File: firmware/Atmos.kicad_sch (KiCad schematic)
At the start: 42 parts, among them J1 AS3935 breakout, J2 BME280 breakout, J3 USB_C_Receptacle_USB2.0_16P, J4 Micro_SD_Card, J5 Solar power input, J6 Conn_Coaxial, Q1 PMOS_Substrate, Q2 PMOS_Substrate, SW2 SW_Push, U1 ESP32-S3-WROOM-1, U10 TPS22918DBVR, U11 MAX17048G_T10, U12 CN3791, U13 SGP40-D-R4, U2 AP2112K-3.3, U3 DS3231M, U4 PMS5003, U5 LTC4412xS6, U7 RFM95W-915S2, U8 USBLC6-2SC6, U9 TPS61023DRLR

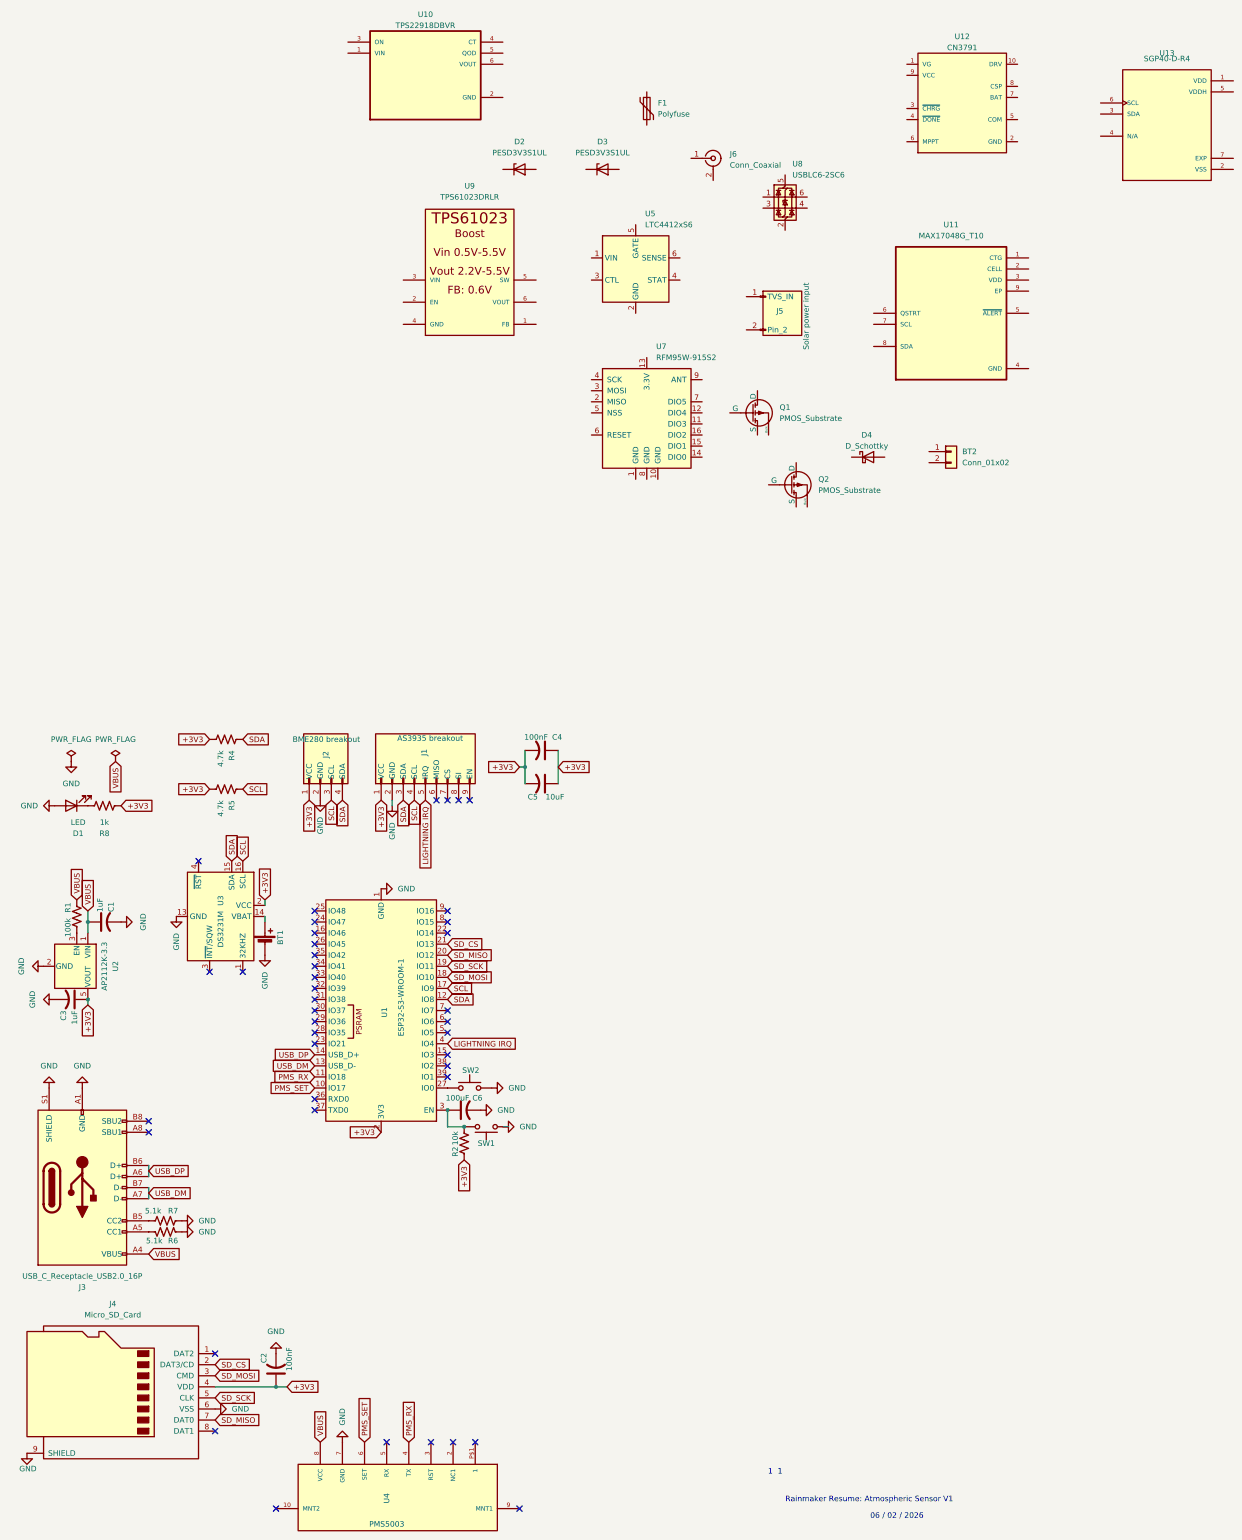
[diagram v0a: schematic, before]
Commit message: Sync latest schematic + add AI exports (PDF/netlist/BOM) for browser-Claude
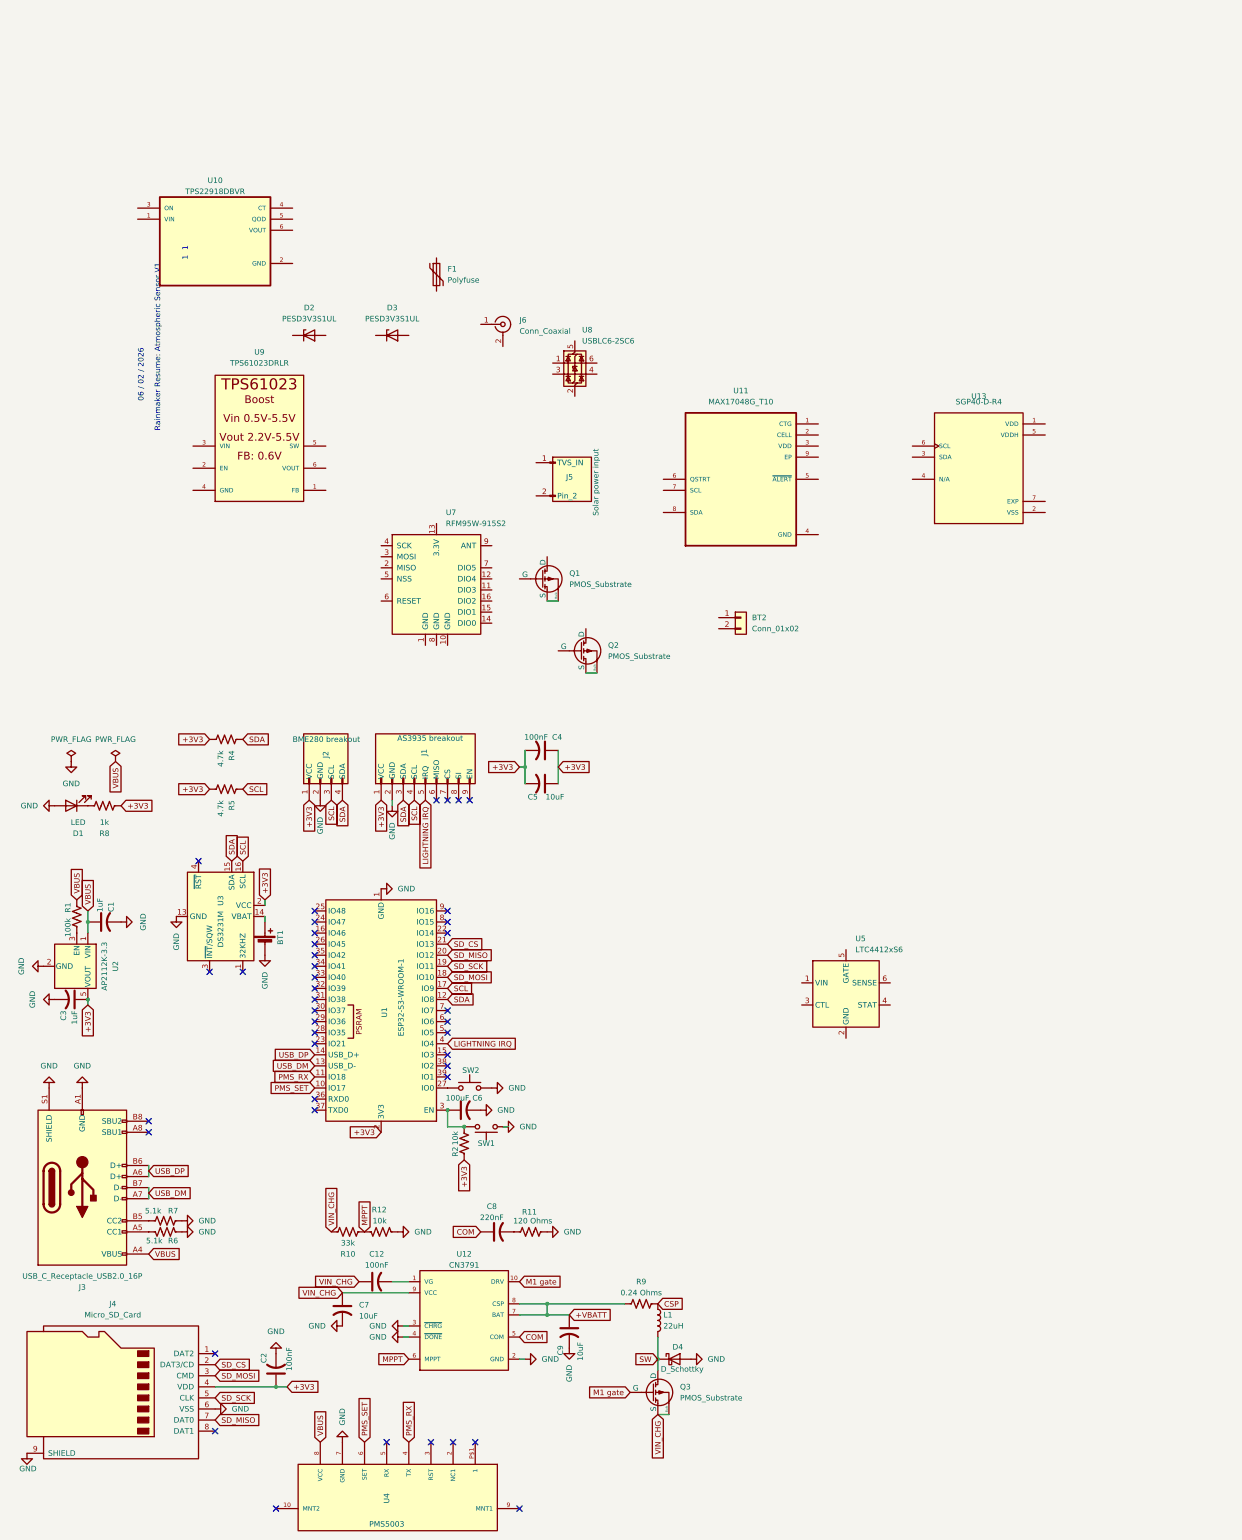
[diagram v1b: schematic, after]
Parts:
- added C12: 100nF, symbol Device:C_US
- added C7, C9: 10uF, symbol Device:C_US
- added C8: 220nF, symbol Device:C_US
- added L1: 22uH, symbol Device:L
- added Q3: PMOS_Substrate, symbol Simulation_SPICE:PMOS_Substrate
- added R10: 33k, symbol Device:R_US
- added R11: 120 Ohms, symbol Device:R_US
- added R12: 10k, symbol Device:R_US
- added R9: 0.24 Ohms, symbol Device:R_US
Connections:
- net GND: now also D4.2 (A), U12.2 (GND), U12.3 (~{CHRG}), U12.4 (~{DONE}), C7.2, C9.2, R11.2, R12.2
- net at Q2.3 (S): now also Q2.4 (Bulk)
- net at Q1.3 (S): now also Q1.4 (Bulk)
- net at U12.1 (VG): now also C12.2
- net M1 gate: now reaches U12.10 (DRV)
- net M1 gate: now also Q3.2 (G)
- net COM: now reaches U12.5 (COM)
- net COM: now also C8.1
- net MPPT: now reaches U12.6 (MPPT)
- net MPPT: now also R10.1, R12.1
- net +VBATT: now reaches U12.7 (BAT)
- net +VBATT: now also U12.8 (CSP), C9.1, R9.1
- net VIN_CHG: now reaches U12.9 (VCC)
- net VIN_CHG: now also C12.1, C7.1, Q3.3 (S), Q3.4 (Bulk), R10.2
- net SW: now reaches D4.1 (K)
- net SW: now also L1.2, Q3.1 (D)
- new net: C8.2, R11.1
- new net CSP: L1.1, R9.2
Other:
- moved on the sheet: BT2, D2, D3, D4, F1, J5, J6, Q1, Q2, U10, U11, U12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

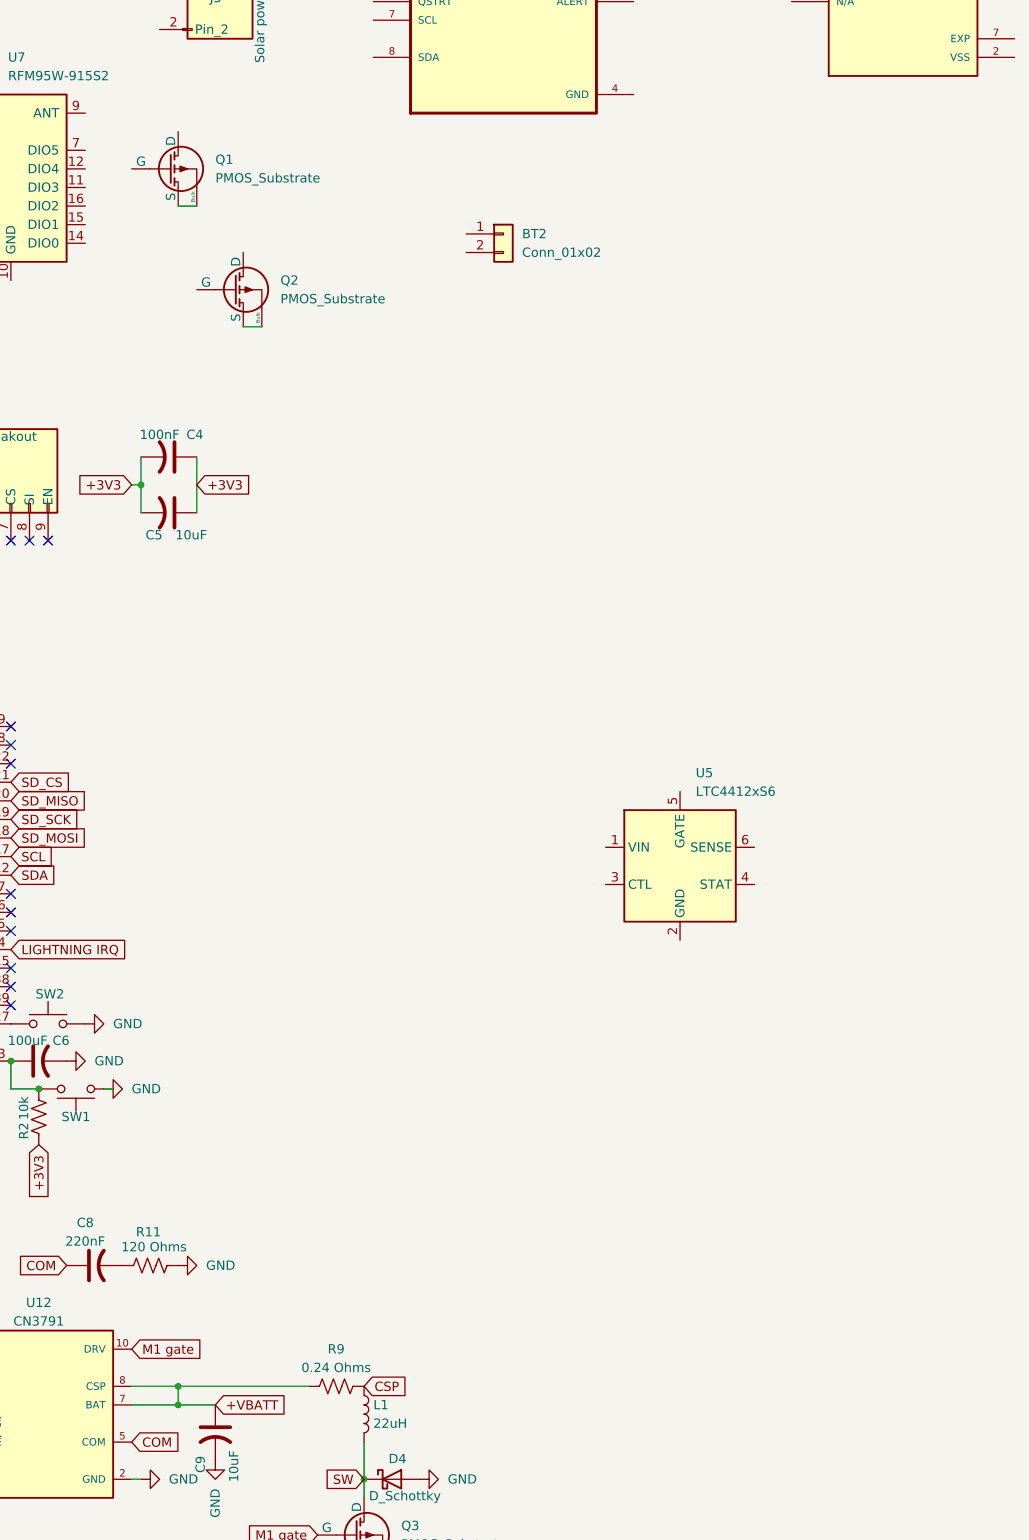
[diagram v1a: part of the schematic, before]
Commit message: U5 LTC4412xS6 wired
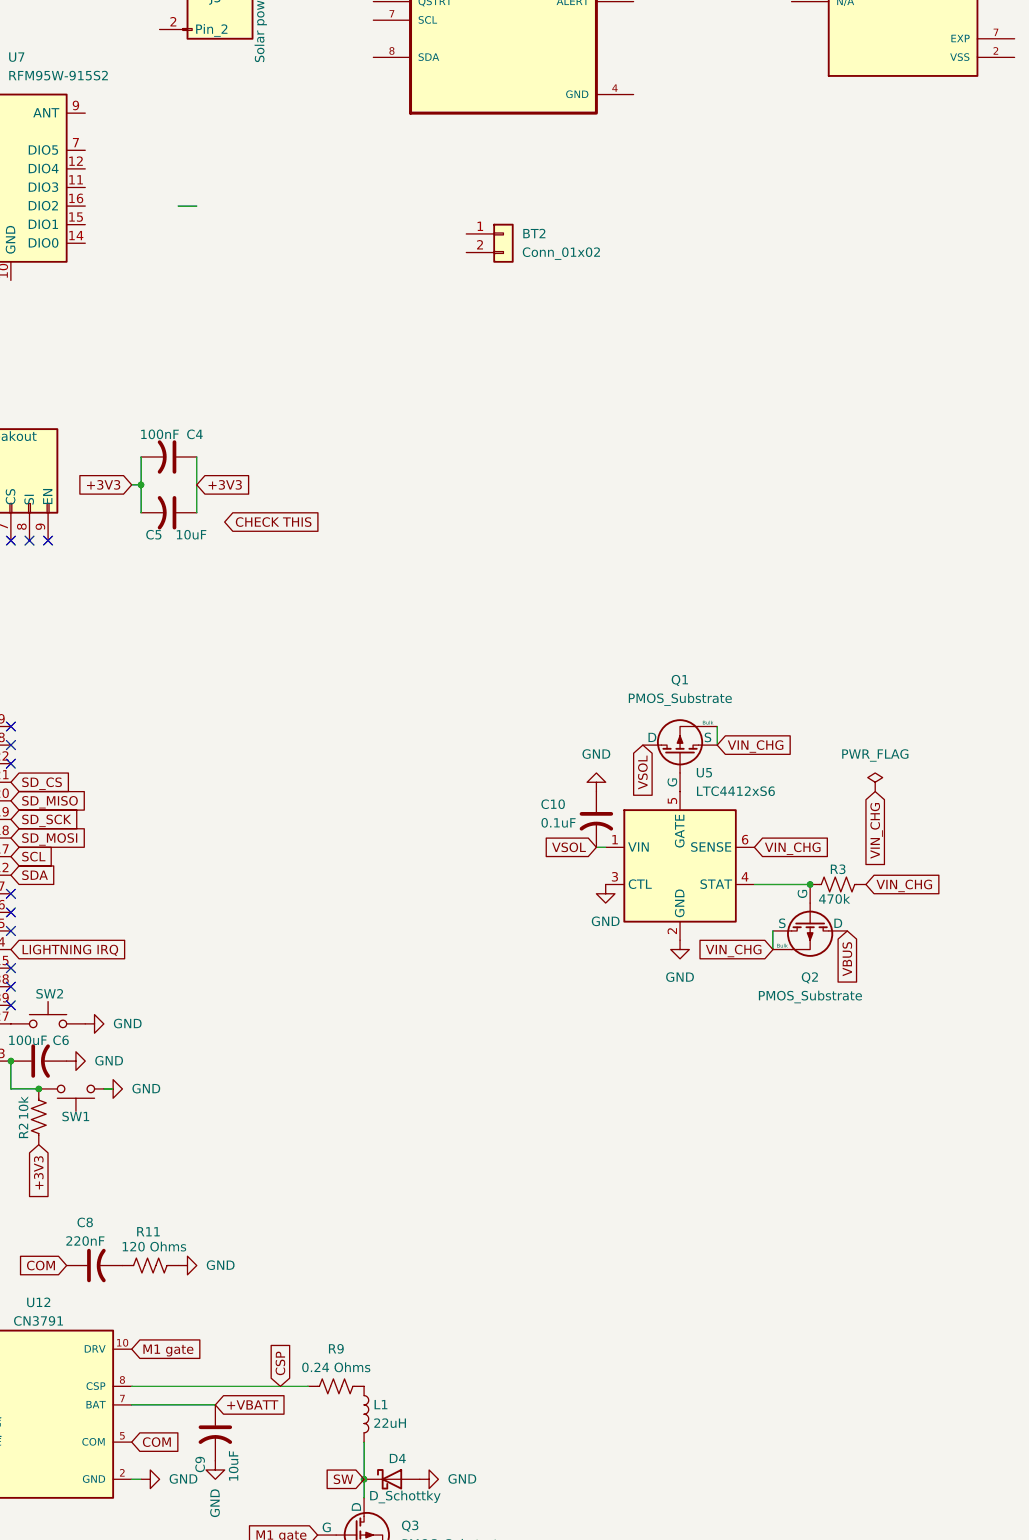
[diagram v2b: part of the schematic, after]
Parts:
- added C10: 0.1uF, symbol Device:C_US
- added R3: 470k, symbol Device:R_US
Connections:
- net +VBATT: no longer R9.1, U12.8 (CSP)
- net CSP: now also R9.1, U12.8 (CSP); no longer L1.1, R9.2
- net GND: now also U5.2 (GND), U5.3 (CTL), C10.1
- net VBUS: now also Q2.1 (D)
- net VIN_CHG: now also Q1.3 (S), Q1.4 (Bulk), Q2.3 (S), Q2.4 (Bulk), U5.6 (SENSE), R3.2
- net at Q2.2 (G): now also U5.4 (STAT), R3.1
- net VSOL: now reaches U5.1 (VIN)
- net VSOL: now also Q1.1 (D), C10.2
- net at U5.5 (GATE): now also Q1.2 (G)
- new net: L1.1, R9.2
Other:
- moved on the sheet: Q1, Q2
